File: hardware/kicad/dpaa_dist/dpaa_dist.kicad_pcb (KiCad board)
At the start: 2 copper layers, 100 x 160 mm, 210 parts, among them J1 2x6, J10 2x6, J11 2x6, J12 2x6, J13 2x6, J14 2x6, J15 2x6, J16 2x6, J17 RJ45, J18 5.5/2.1, J2 2x6, J20 IDC 2x15, J21 IDC 2x15, J25 ESP32, J26 3.5mm, J27 3.5mm, J3 2x6, J4 2x6, J5 2x6, J6 2x6, J7 2x6, J8 2x6, J9 2x6, Q1 AO4407A, SW1 кнопка, U1 74LVC244A, U10 74LVC244A, U11 74LVC244A, U12 74LVC244A, U13 74LVC244A, U2 74LVC244A, U20 AP2112K-3.3, U21 AP2112K-3.3, U3 74LVC244A, U31 PCM5102A, U32 TDA1308, U4 74LVC244A, U5 74LVC244A, U6 74LVC244A, U7 74LVC244A, U8 74LVC244A, U9 74LVC244A

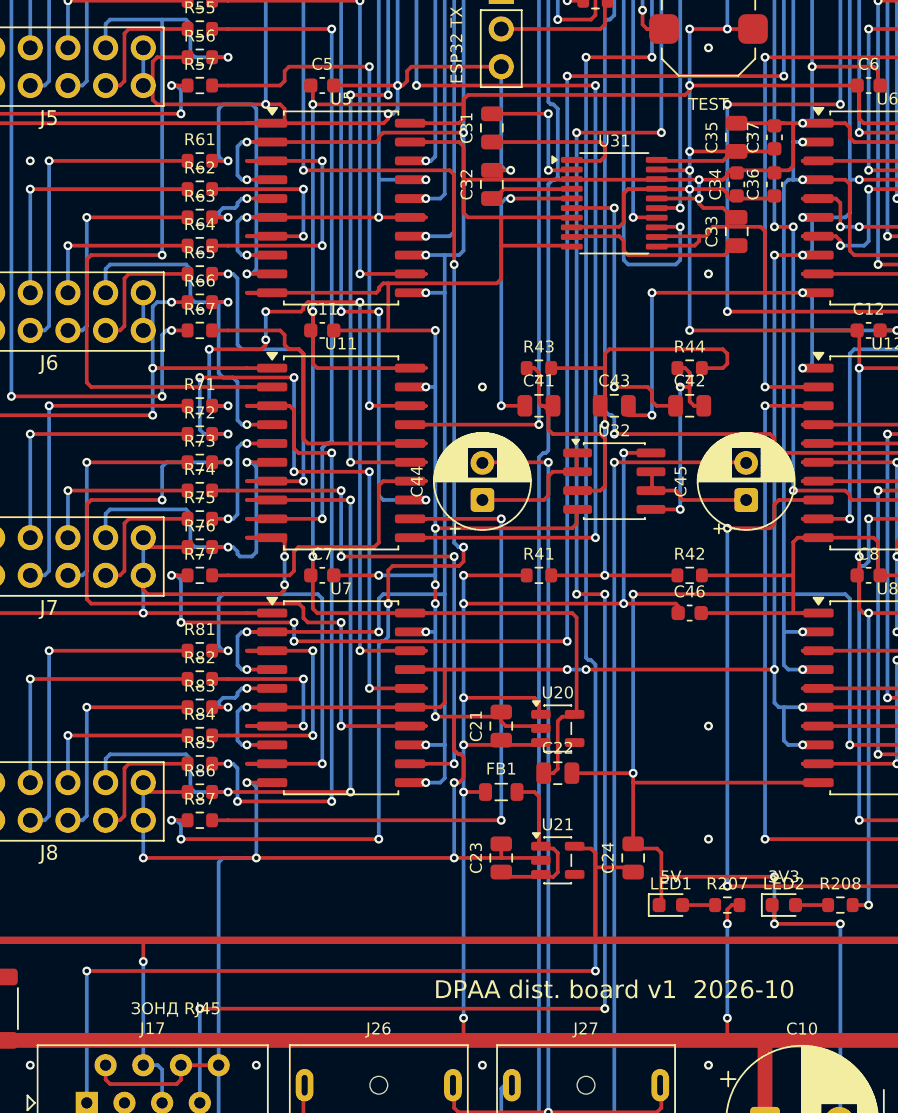
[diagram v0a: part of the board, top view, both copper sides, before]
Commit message: Распределительная плата: журнал скоса углов, шелкография >=1 мм, нормы заказа в README
Co-Authored-By: Claude Fable 5.1 <noreply@anthropic.com>
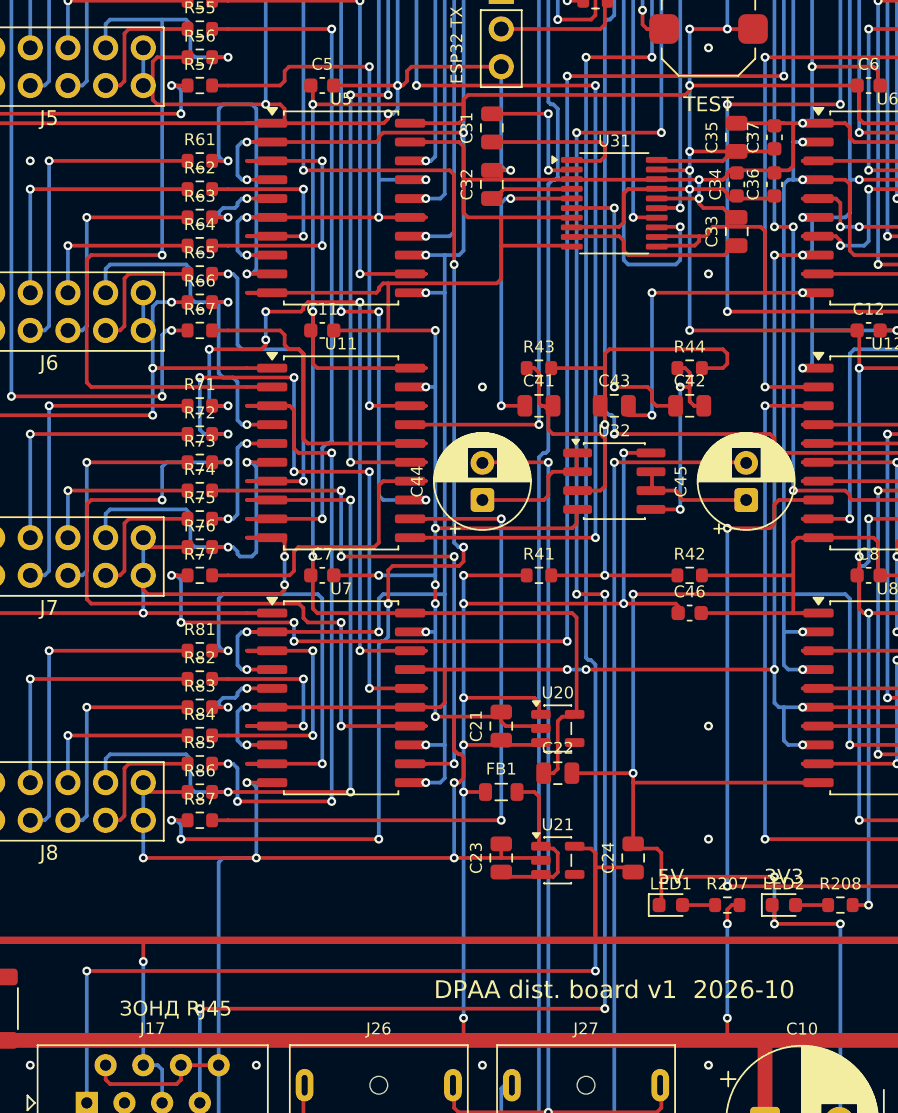
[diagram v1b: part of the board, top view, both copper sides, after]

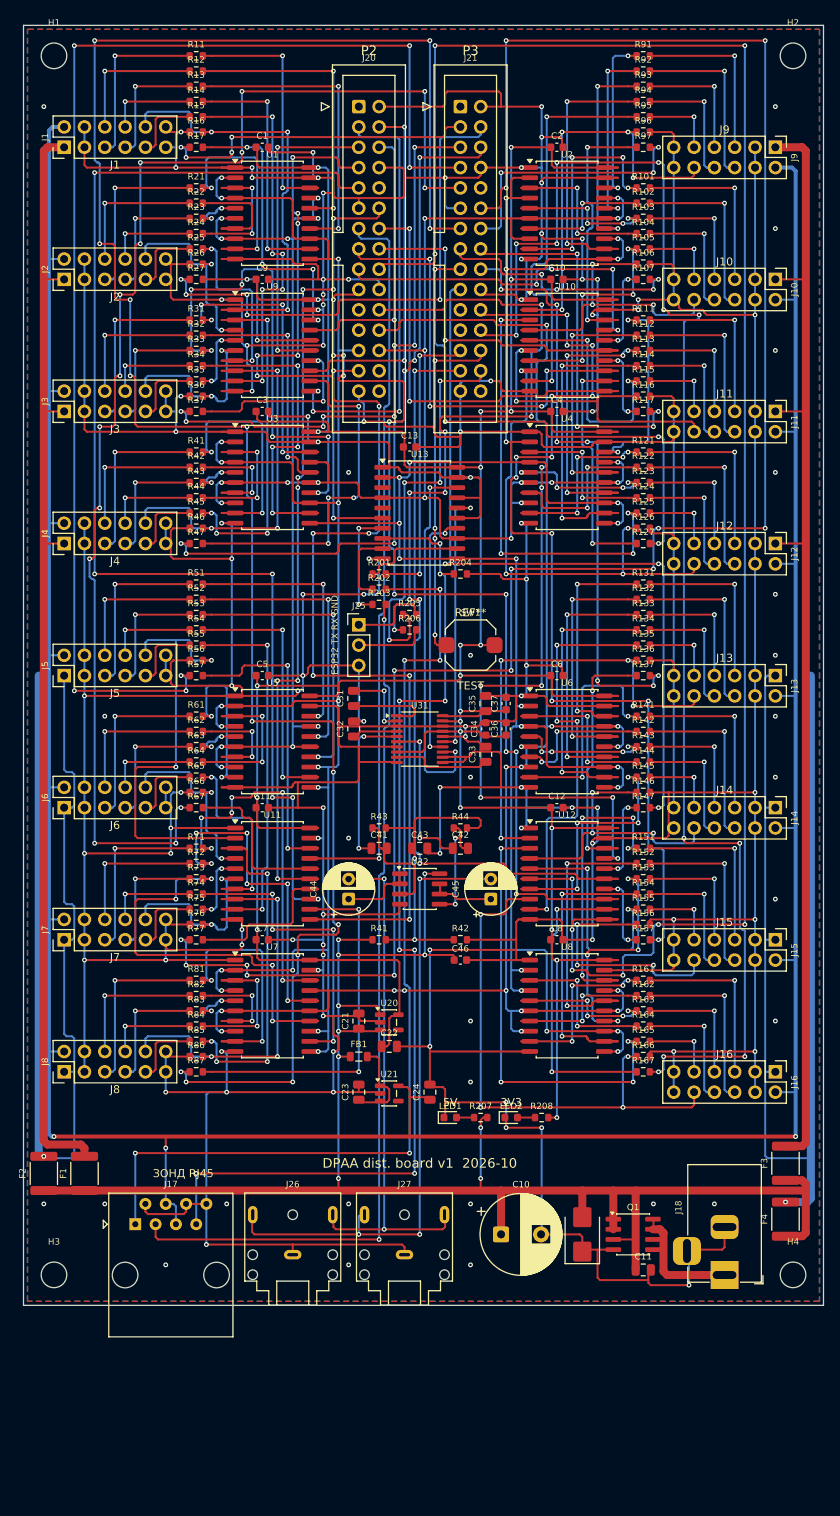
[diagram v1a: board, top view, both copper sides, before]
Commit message: Распределительная плата: порт Ethernet (P1 -> MagJack), плата 100x180, исправлена нумерация вилок IDC
- J19 = гребёнка P1 платы расширения (третий прямой шлейф IDC 2x15), J29 = RJ45 MagJack
  UDE RB1-125B8G1A (1000BASE-T, трансформаторы и терминация Боба Смита внутри, общий вывод
  и экран — на отдельную цепь CHASSIS: полигон под гнездом на обоих слоях, к земле через
  C306 1 нФ 2 кВ || R306 1 МОм); центральный отвод — C301 100 нФ, R301 0 Ом (DNP) к 3,3 В.
- Пары MDI разведены вручную одним слоем каждая (пары 1, 2 — верх, 3, 4 — низ), 45°, без
  переходных, сплошная земля другого слоя под ними, прочие цепи не ближе 1 мм; пары 2 и 4 —
  с обратной полярностью (без пересечений; PHY исправляет полярность). Расчёт волнового
  сопротивления и длины линий — README, gen/eth_lengths.txt.
- Исправлено: контакты вилок J20/J21 (и J19) теперь назначены с учётом зигзаг-нумерации
  футпринта IDC против нумерации 1-15/16-30 гребёнок платы расширения (прямой шлейф
  соединяет по положению); раньше сигналы стояли на чужих контактах.
- Плата 100x180: краевые разъёмы сдвинуты вниз, шина +5 В обходит MagJack по краю и ныряет
  под VIN через переходные; силовые C10/C11 переименованы в C101/C102 (дублировали C10/C11
  буферов); переходные земли у каждого конденсатора развязки; земля вилок через заливку
  (запрет вертикали между рядами J20/J21), автосшивка кусков земли (gen/stitch_fix.py).
- DRC: 0 ошибок, 0 неподключённых (4 предупреждения: концы шин 5V_B/5V_D, узкие перешейки
  заливки); ERC 0. Пакет fab/ перегенерирован; BOM: J29 C363353, C306 C135917, R301 исключён.
- Документация: README (раздел Ethernet, нумерация шлейфов), purchase.md (3 шлейфа, MagJack),
  wiring.md (W3, W29), bom.csv, schematics.md.

Co-Authored-By: Claude Fable 5.1 <noreply@anthropic.com>
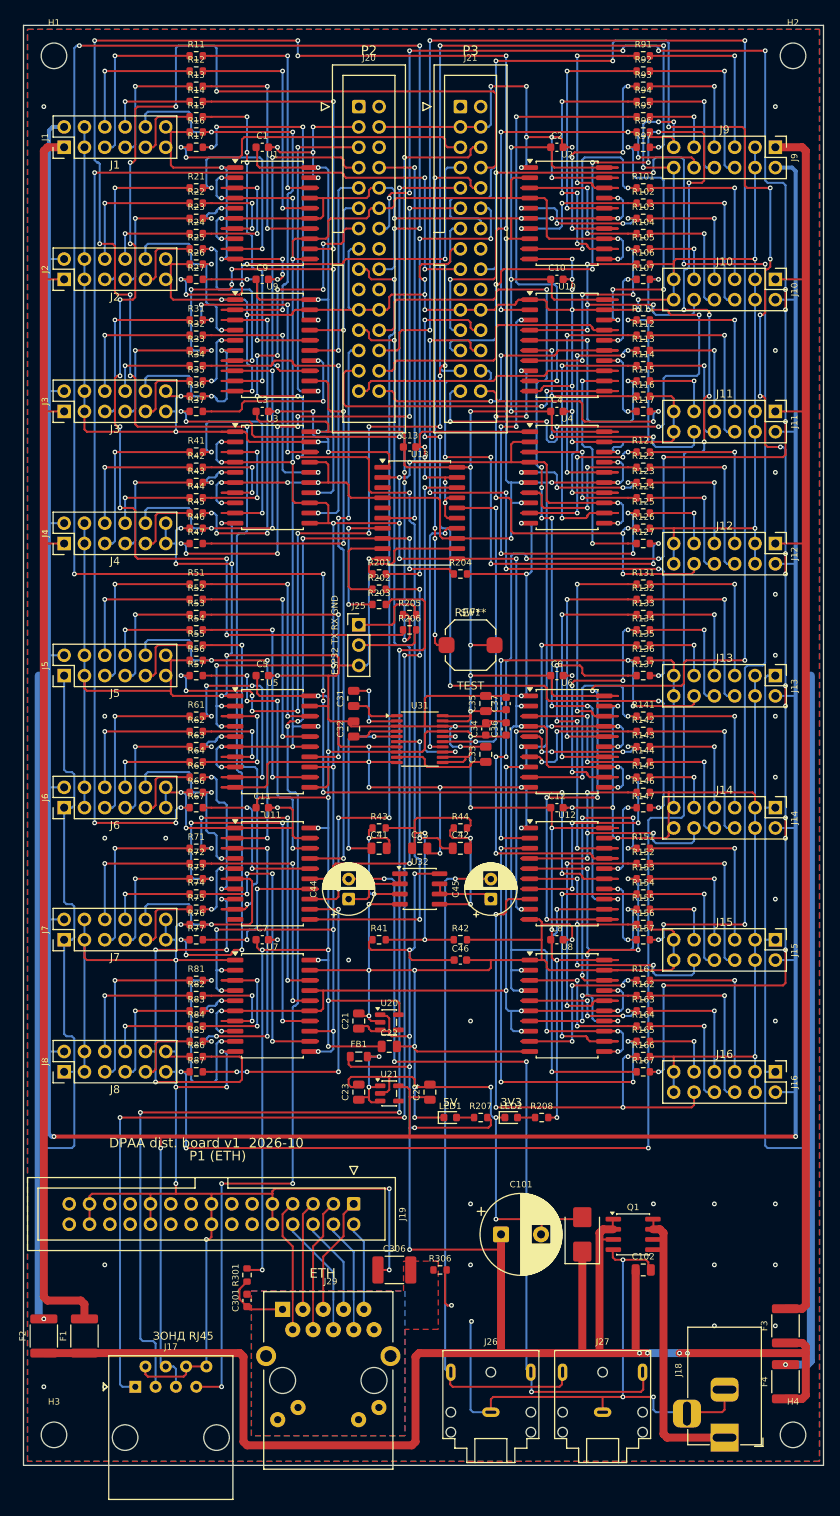
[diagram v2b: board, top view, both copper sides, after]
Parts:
- removed the C10 at (59.7, 151.1)
- removed the C11 at (77.5, 155.6)
- added C101: 1000u, CP_Radial_D10.0mm_P5.00mm, F.Cu at (59.7, 151.1)
- added C102: 10u, C_0805_2012Metric, F.Cu at (77.5, 155.6)
- added C301: 100n, C_0603_1608Metric, F.Cu at (27.9, 159.4)
- added C306: 1n 2kV, C_1812_4532Metric, F.Cu at (46.4, 155.6)
- added J19: IDC 2x15, IDC-Header_2x15_P2.54mm_Vertical, F.Cu at (41.3, 147.3)
- added J29: RB1-125B8G1A, RJ45_UDE_RB1-125B8G1A, F.Cu at (32.4, 160.5)
- added R301: 0R DNP, R_0603_1608Metric, F.Cu at (27.9, 156.2)
- added R306: 1M, R_0603_1608Metric, F.Cu at (52.1, 155.6)
- moved J26 31.6 mm to (58.4, 173.4)
- moved J27 31.6 mm to (72.4, 173.4)
- moved F1 20.3 mm to (7.62, 163.8)
- moved F2 20.3 mm to (2.54, 163.8)
- moved F3 20.3 mm to (95.2, 162.6)
- moved F4 20.3 mm to (95.2, 169.5)
- moved J17 20.3 mm to (14.0, 170.2)
- moved J18 20.3 mm to (87.6, 176.5)
- moved H3 20.0 mm to (3.81, 176.2)
- moved H4 20.0 mm to (96.2, 176.2)
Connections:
- D1 pad 1: GND -> +5V
- D1 pad 2: +5V -> GND
- J20 pad 10: (no net) -> LRCLK
- J20 pad 11: GND -> TXD3
- J20 pad 12: TXD6 -> BCLK
- J20 pad 13: TXD7 -> TXD4
- J20 pad 14: TXD8 -> TXD15
- J20 pad 15: TXD9 -> GND
- J20 pad 16: TXD10 -> (no net)
- J20 pad 17: TXD11 -> TXD5
- J20 pad 18: TXD12 -> TXD14
- J20 pad 19: TXD13 -> (no net)
- J20 pad 2: GND -> (no net)
- J20 pad 20: GND -> (no net)
- J20 pad 21: (no net) -> GND
- J20 pad 22: TXD14 -> GND
- J20 pad 23: (no net) -> TXD6
- J20 pad 24: TXD15 -> TXD13
- J20 pad 25: BCLK -> TXD7
- J20 pad 26: LRCLK -> TXD12
- J20 pad 27: MON_SD -> TXD8
- J20 pad 28: (no net) -> TXD11
- J20 pad 29: GND -> TXD9
- J20 pad 3: TXD0 -> GND
- J20 pad 30: (no net) -> TXD10
- J20 pad 4: TXD1 -> GND
- J20 pad 5: TXD2 -> TXD0
- J20 pad 6: TXD3 -> (no net)
- J20 pad 7: TXD4 -> TXD1
- J20 pad 8: GND -> MON_SD
- J20 pad 9: TXD5 -> TXD2
- J21 pad 10: (no net) -> BTN_TEST
- J21 pad 11: GND -> MIC3
- J21 pad 12: MIC6 -> CAL
- J21 pad 13: MIC7 -> MIC4
- J21 pad 14: MIC8 -> MIC15
- J21 pad 15: MIC9 -> GND
- J21 pad 16: MIC10 -> (no net)
- J21 pad 17: MIC11 -> MIC5
- J21 pad 18: MIC12 -> MIC14
- J21 pad 19: MIC13 -> (no net)
- J21 pad 2: GND -> (no net)
- J21 pad 20: GND -> (no net)
- J21 pad 21: (no net) -> GND
- J21 pad 22: MIC14 -> GND
- J21 pad 23: (no net) -> MIC6
- J21 pad 24: MIC15 -> MIC13
- J21 pad 25: CAL -> MIC7
- J21 pad 26: BTN_TEST -> MIC12
- J21 pad 27: ESP_RX -> MIC8
- J21 pad 28: ESP_TX -> MIC11
- J21 pad 29: GND -> MIC9
- J21 pad 3: MIC0 -> GND
- J21 pad 30: (no net) -> MIC10
- J21 pad 4: MIC1 -> GND
- J21 pad 5: MIC2 -> MIC0
- J21 pad 6: MIC3 -> ESP_TX
- J21 pad 7: MIC4 -> MIC1
- J21 pad 8: GND -> ESP_RX
- J21 pad 9: MIC5 -> MIC2
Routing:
- net ESP_RX: track 41.6 -> 174.2 mm, vias 2 -> 10
- net TXD14: track 138.3 -> 249.4 mm, vias 8 -> 11
- net TXD15: track 117.5 -> 227.4 mm, vias 8 -> 15
- net GND: track 1644.6 -> 1560.3 mm, vias 127 -> 130
- net +5V: track 218.1 -> 294.3 mm
- net MIC4: track 161.6 -> 99.8 mm, vias 6 -> 11
- net TXD5: track 154.2 -> 93.0 mm, vias 6 -> 4
- net MIC8: track 33.1 -> 85.2 mm
- net MIC14: track 122.6 -> 160.7 mm, vias 12 -> 7
- net HP_L: track 65.7 -> 102.9 mm, vias 2 -> 4
- net MIC9: track 31.3 -> 66.3 mm, vias 4 -> 7
- net 3V3L: track 470.8 -> 505.2 mm, vias 22 -> 27
- net MIC15: track 183.0 -> 214.6 mm, vias 12 -> 17
- net LRC_P: track 110.1 -> 140.6 mm, vias 2 -> 3
- net TXD4: track 157.3 -> 132.8 mm, vias 12 -> 10
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- added copper zone on B.Cu, net CHASSIS
- added copper zone on F.Cu, net CHASSIS
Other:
- board size 100 x 160 mm -> 100 x 180 mm
- board text added: "ETH"
- board text added: "P1 (ETH)"
